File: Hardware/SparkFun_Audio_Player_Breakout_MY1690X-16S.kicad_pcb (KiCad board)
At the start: 4 copper layers, 25.4 x 25.4 mm, 67 parts, among them J1 3.5mm TRRS, J2 Conn_01x03, J3 Conn_01x02, J4 USB_C_Receptacle, J5 Conn_01x06, J6 microSD, Q1 BSS138, U2 MY1690X-16S

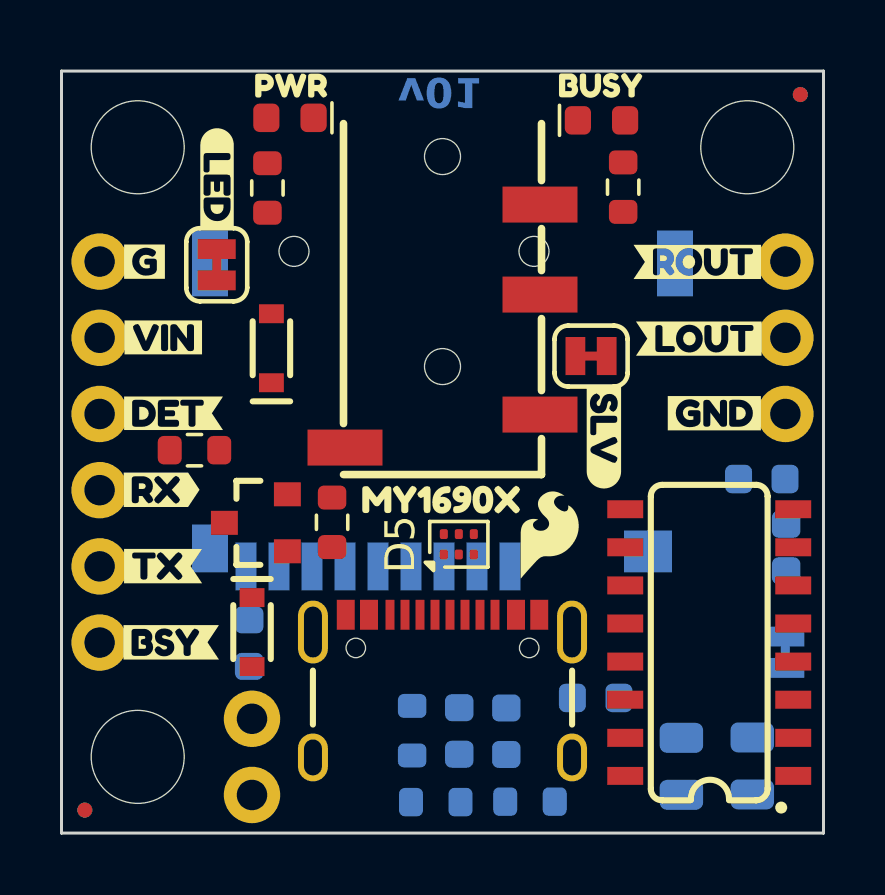
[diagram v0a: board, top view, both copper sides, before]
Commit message: re-order header pins to put GND/VIN/RX/TX in a row
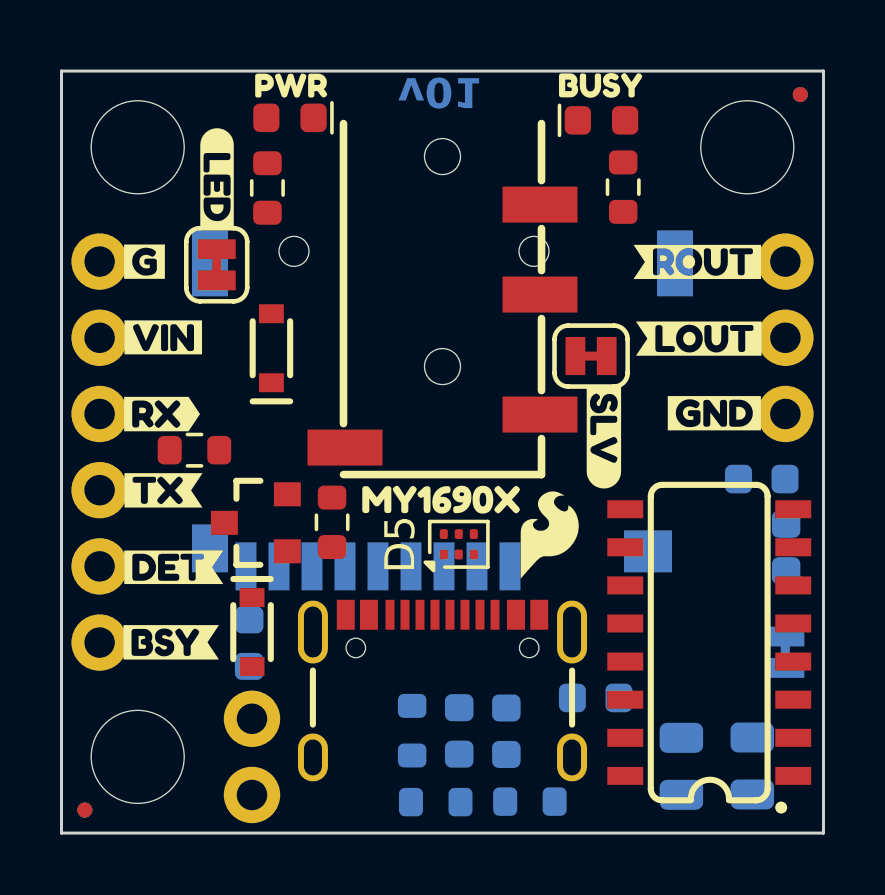
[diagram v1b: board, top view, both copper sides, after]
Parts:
- removed kibuzzard-6792CCC6: G***, kibuzzard-6792CCC6
- added kibuzzard-6793B9F5: G***, kibuzzard-6793B9F5, B.Cu at (137.7, 107.9)
- moved kibuzzard-6792C89C 5.13 mm to (138.4, 108.0)
- moved kibuzzard-6792CCE2 2.56 mm to (138.0, 102.9)
- moved kibuzzard-6792CCF2 2.56 mm to (137.8, 105.4)
- moved kibuzzard-6792C82F 2.52 mm to (138.0, 102.9)
- moved kibuzzard-6792C85C 2.52 mm to (138.0, 105.4)
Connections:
- J5 pad 3: SD_DET -> MY_RX
- J5 pad 4: MY_RX -> MY_TX
- J5 pad 5: MY_TX -> SD_DET

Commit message: TVS diode SOT23-6 package
-for easier production/rework
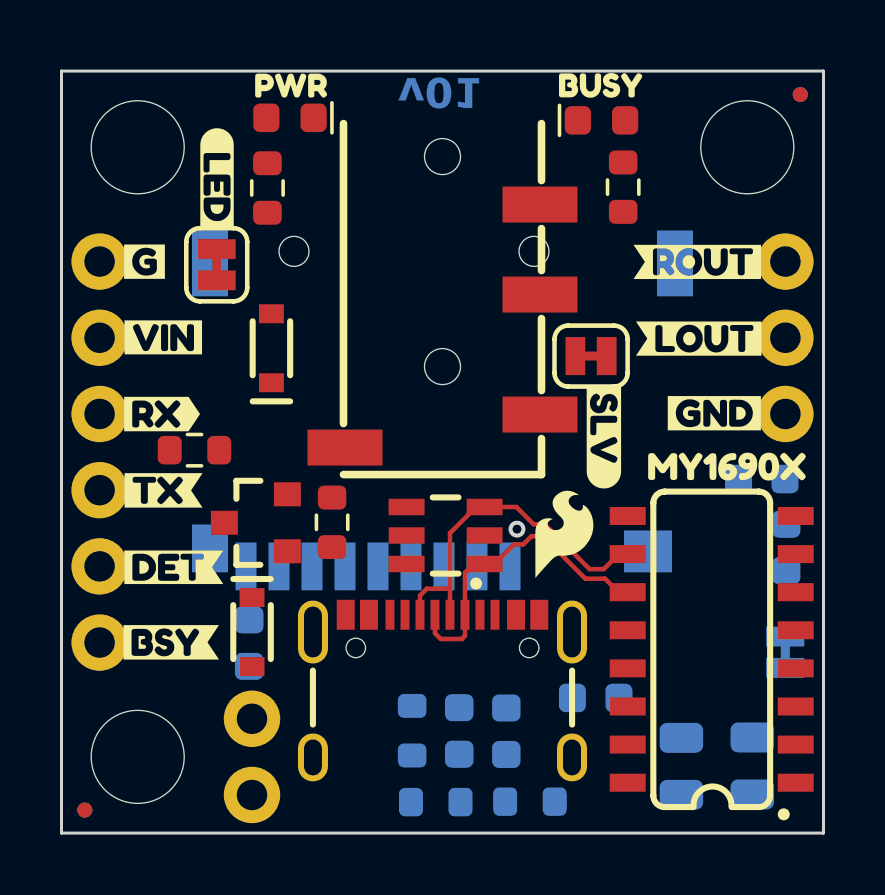
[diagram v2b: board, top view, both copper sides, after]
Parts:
- removed D5: PRTR5V0U2F, Package_TO_SOT_SMD:SOT-886
- added D6: DT1042-04SO, SparkFun-Semiconductor-Standard:SOT23-6, F.Cu at (147.4, 106.9)
- moved kibuzzard-6792C7DD 9.59 mm to (156.8, 104.6)
- moved G*** 0.49 mm to (151.4, 106.9)
- moved U2 0.24 mm to (156.3, 110.7)
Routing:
- net Net-(D6-I/O2): track 0.00 -> 11.8 mm
- net Net-(D6-I/O1): track 0.00 -> 10.5 mm
- net GND: vias 0 -> 1

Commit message: Routed v01 (pre-review)
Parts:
- added C6: 10uF, SparkFun-Capacitor:C_0603_1608Metric, B.Cu at (159.1, 113.6)
- added C9: 0.1uF, SparkFun-Capacitor:C_0603_1608Metric, B.Cu at (157.1, 107.5)
- added kibuzzard-679417DC: G***, kibuzzard-679417DC, F.Cu at (143.3, 98.3)
- moved R4 1.95 mm to (140.8, 103.1), turned to 0 degrees
- moved C4 1.29 mm to (156.4, 114.6)
- moved C5 1.00 mm to (154.3, 114.6)
- moved Q1 0.76 mm to (140.9, 105.8), turned to 90 degrees
- moved R1 0.48 mm to (143.2, 106.7), turned to 90 degrees
- moved C8 0.40 mm to (159.2, 107.4)
- moved C7 0.39 mm to (158.3, 105.2)
- moved C1 0.34 mm to (152.2, 112.0)
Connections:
- JP2 pad 2: 3.3V_P -> VCC
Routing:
- net BUSY: track 0.00 -> 31.9 mm, vias 0 -> 2
- net 3.3V_P: track 0.00 -> 31.8 mm, vias 0 -> 3
- net DAC_R: track 0.00 -> 26.3 mm
- net SD_CLK: track 0.00 -> 25.6 mm, vias 0 -> 1
- net DAC_L: track 0.00 -> 23.3 mm, vias 0 -> 1
- net MY_TX: track 0.00 -> 22.7 mm
- net SD_DAT: track 0.00 -> 20.7 mm, vias 0 -> 1
- net Net-(JP1-A): track 0.00 -> 19.7 mm, vias 0 -> 3
- net MY_RX_LV: track 0.00 -> 18.4 mm
- net Net-(D2-K): track 0.00 -> 16.6 mm, vias 0 -> 2
- net SD_CMD: track 0.00 -> 15.7 mm, vias 0 -> 1
- net Net-(J4-CC2): track 0.00 -> 12.6 mm, vias 0 -> 1
- net VCC: track 0.00 -> 11.7 mm, vias 0 -> 5
- net VUSB: track 0.00 -> 11.2 mm, vias 0 -> 2
- net Net-(JP3-A): track 0.00 -> 8.94 mm
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- added copper zone on F.Cu, net VUSB

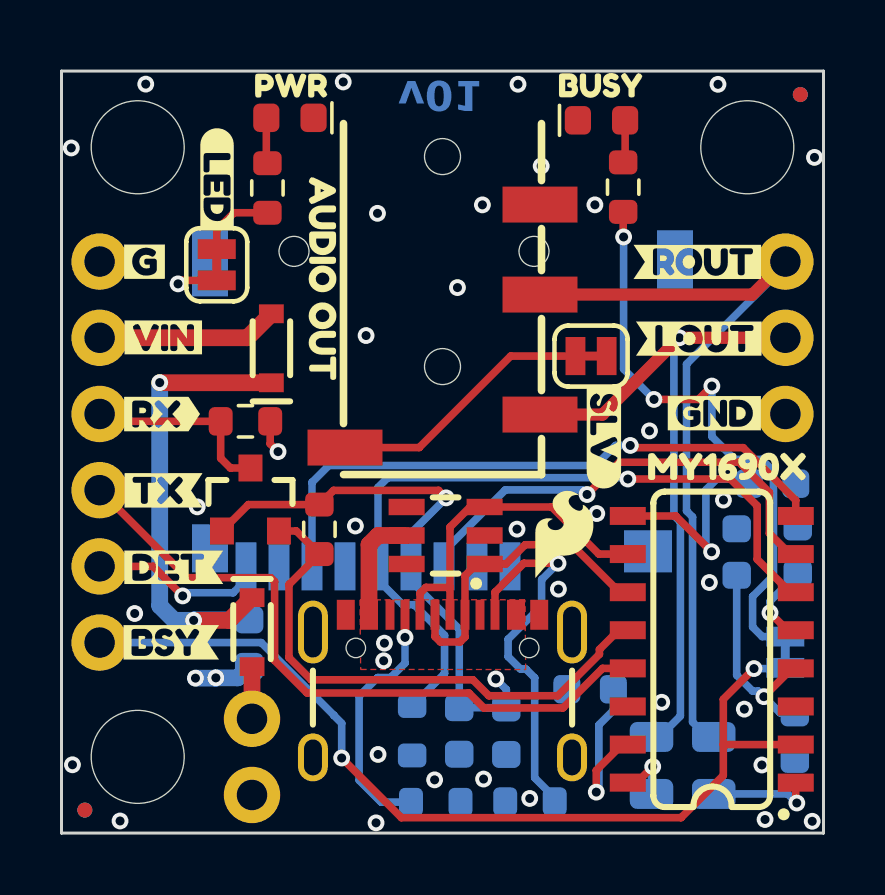
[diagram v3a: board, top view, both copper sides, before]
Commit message: review changes 1
-TX bottom silk fishtail (output)
-centered position of OSHW logo
-nudged vcc vias near VUSB pth headers for better ground flow pour
-named JP3 "SLV"
-added jumper comments to sch
-moved C1/C8 to avoid text overlap in SCH
-added RD to jumpers in sch
-added NC flags to unused pins on SCH
-measures
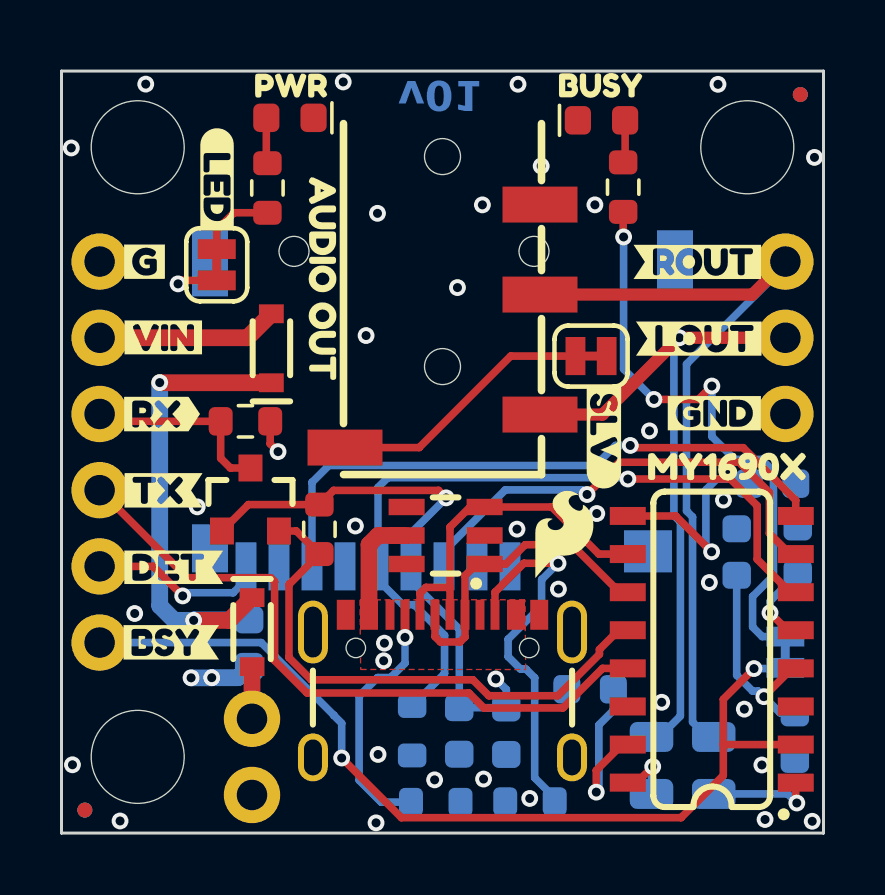
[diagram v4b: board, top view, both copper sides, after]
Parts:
- removed kibuzzard-6792CCF2: G***, kibuzzard-6792CCF2
- added kibuzzard-6798FF71: G***, kibuzzard-6798FF71, B.Cu at (138.0, 105.4)
- JP3: value ~ -> SLV
- moved Ref** 0.15 mm to (147.3, 110.6)
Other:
- board text added: "Inner Copper Weight: 0.5oz"
- board text added: "Layers: 4"
- board text removed: "Layers: 2"

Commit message: removed R6 pull-down on uSD CLK line
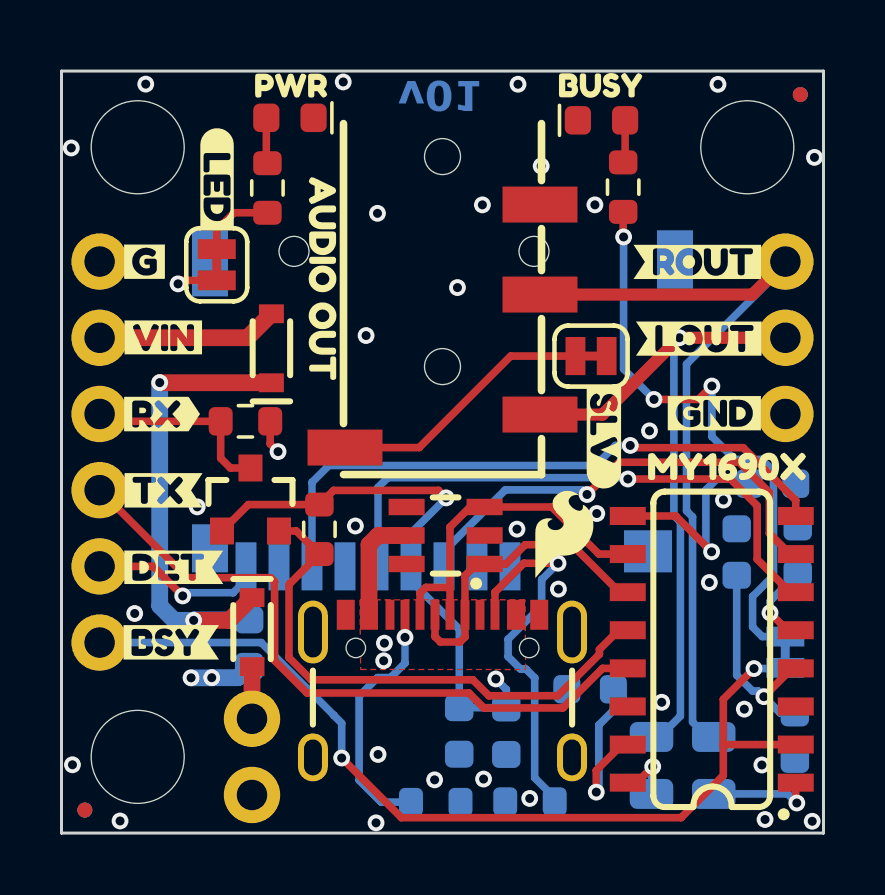
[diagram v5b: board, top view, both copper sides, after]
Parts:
- removed R6: 1k, SparkFun-Resistor:R_0603_1608Metric
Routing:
- net SD_CLK: track 25.6 -> 19.3 mm

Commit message: review changes 2
-rotated LED jumper for easier access to cut when headers are populated
-repositioned bottom passive components under the USB (now that R6 is gone). This allows bypass caps to be closer to uSD card pins.
-updated frame info on brd and sch
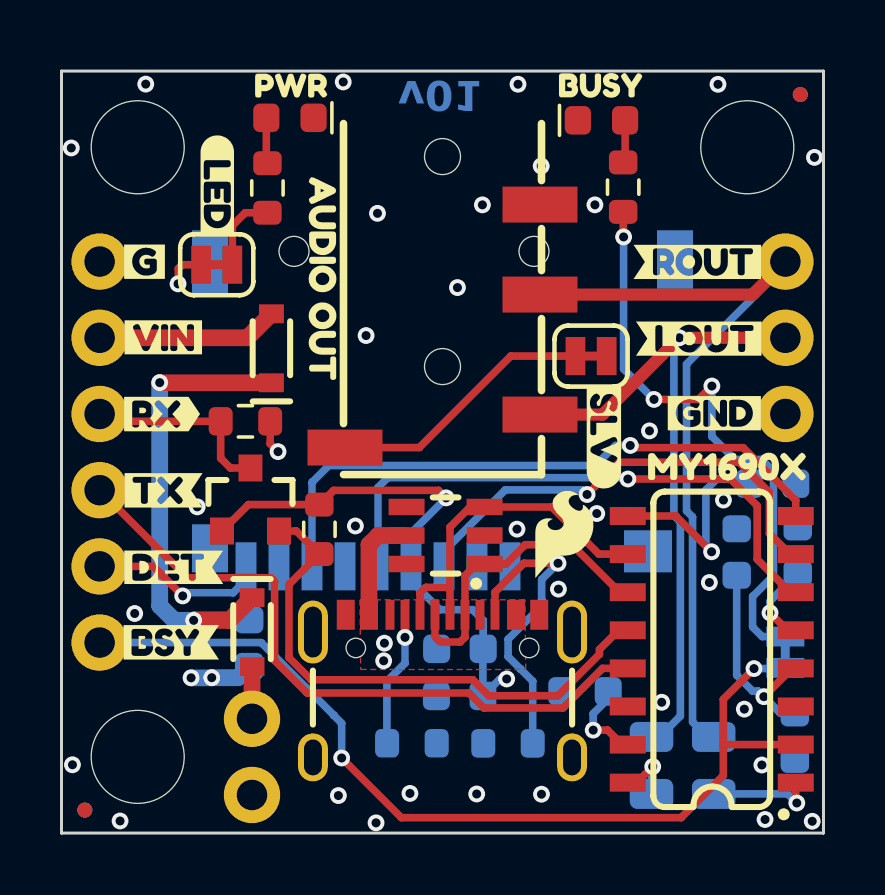
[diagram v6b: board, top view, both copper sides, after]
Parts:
- moved Ref** 5.22 mm to (147.3, 115.8)
- moved C3 2.74 mm to (147.9, 110.7), turned to 180 degrees
- moved R3 2.12 mm to (146.3, 113.8)
- moved R2 2.07 mm to (149.5, 113.8)
- moved C2 1.95 mm to (147.9, 112.3), turned to 180 degrees
- moved G1 1.47 mm to (216.1, 168.0)
- moved kibuzzard-6792CF7B 0.24 mm to (139.8, 95.3)
- moved C1 0.18 mm to (152.1, 112.1)
- turned JP2 to 180 degrees
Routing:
- net Net-(J4-CC1): track 8.43 -> 4.48 mm
- net Net-(U2-VPN): track 5.79 -> 2.99 mm
- net Net-(J4-CC2): track 12.6 -> 10.3 mm
- net 3.3V_P: track 31.8 -> 30.4 mm
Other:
- board text added: "Ordering Notes:"
- board text added: "Solder Mask: Black"
- board text removed: "Ordering Notes"
- board text removed: "Solder Mask: Red"

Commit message: repositioned connectors to have over-hang
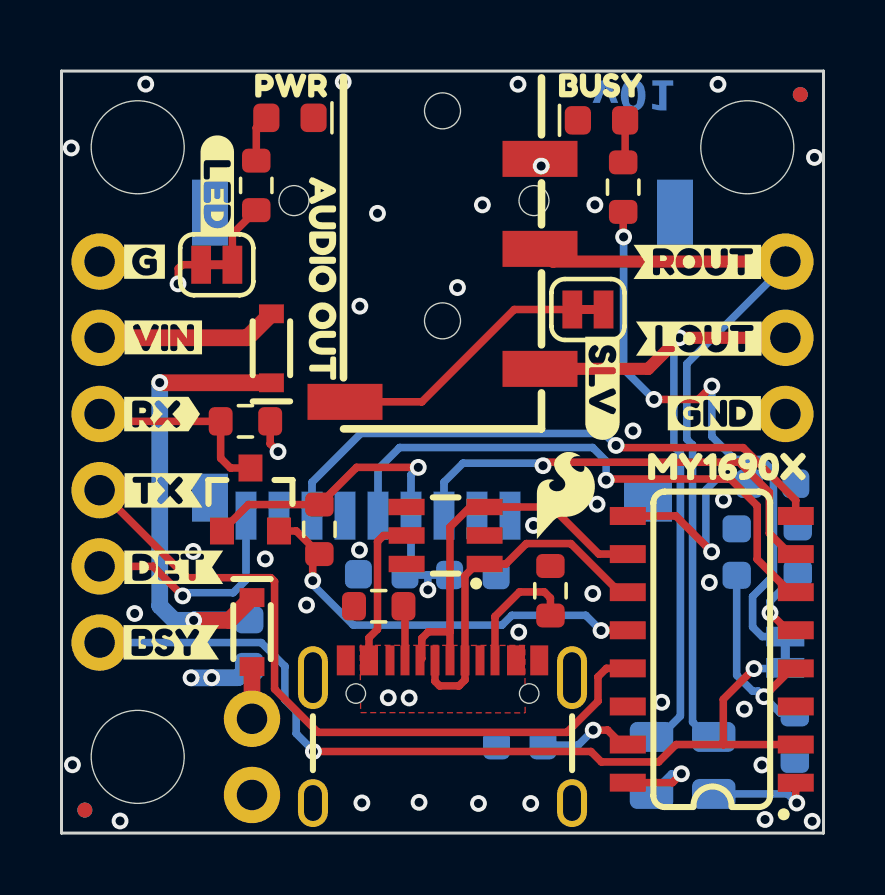
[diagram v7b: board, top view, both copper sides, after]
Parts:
- R2, R3: moved to F.Cu
- moved R2 5.28 mm to (150.9, 108.8), turned to 90 degrees
- moved R3 4.70 mm to (145.2, 109.3), turned to 0 degrees
- moved Ref** 4.68 mm to (147.3, 111.1)
- moved C2 4.05 mm to (148.3, 108.2), turned to 0 degrees
- moved C3 3.60 mm to (145.3, 108.2)
- moved C1 2.82 mm to (149.9, 113.9)
- moved kibuzzard-6792CAD9 2.07 mm to (145.2, 114.8)
- moved kibuzzard-6792CAB7 1.99 mm to (145.5, 113.4)
- moved J6 1.69 mm to (147.3, 95.8)
- moved kibuzzard-6792CF8E 1.62 mm to (152.7, 102.0)
- moved JP3 1.56 mm to (152.2, 99.4), turned to 180 degrees
- moved J1 1.52 mm to (147.3, 96.3)
- moved J4 1.52 mm to (147.3, 110.7)
- moved G*** 1.30 mm to (151.4, 105.6)
- moved R9 0.38 mm to (141.1, 95.3)
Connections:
- J1 pad S: Net-(JP3-A) -> Net-(JP3-B)
- JP3 pad 1: Net-(JP3-A) -> GND
- JP3 pad 2: GND -> Net-(JP3-B)
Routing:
- net Net-(JP3-A): track 8.94 -> 0.00 mm
- net Net-(JP3-B): track 0.00 -> 8.85 mm
- net Net-(J4-CC2): track 10.3 -> 4.32 mm, vias 1 -> 0
- net MY_RX_LV: track 18.4 -> 14.2 mm, vias 0 -> 2
- net VUSB: track 11.2 -> 15.2 mm
- net Net-(J4-CC1): track 4.48 -> 1.83 mm, vias 1 -> 0
- net 3.3V_P: track 30.4 -> 28.5 mm
- net BUSY: track 31.9 -> 30.2 mm
- net MY_TX: track 22.7 -> 24.4 mm
- net SD_DET: track 5.96 -> 7.65 mm
- net Net-(D6-I/O2): track 11.6 -> 13.1 mm
- net Net-(D6-I/O1): track 10.4 -> 11.9 mm
- net SD_DAT: track 20.7 -> 19.4 mm
- net Net-(U2-DACL): track 1.98 -> 3.19 mm
- net DAC_L: track 23.3 -> 22.6 mm
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- added copper zone on In1.Cu, net VUSB

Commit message: checklist eng run
-added ordering instruction about NPTH holes (under the TRRS connector)
-sch cleanup
-add VIN range in SCH and BRD
-add "1234" text objects to each layer
-nudges a via under LOUT silk
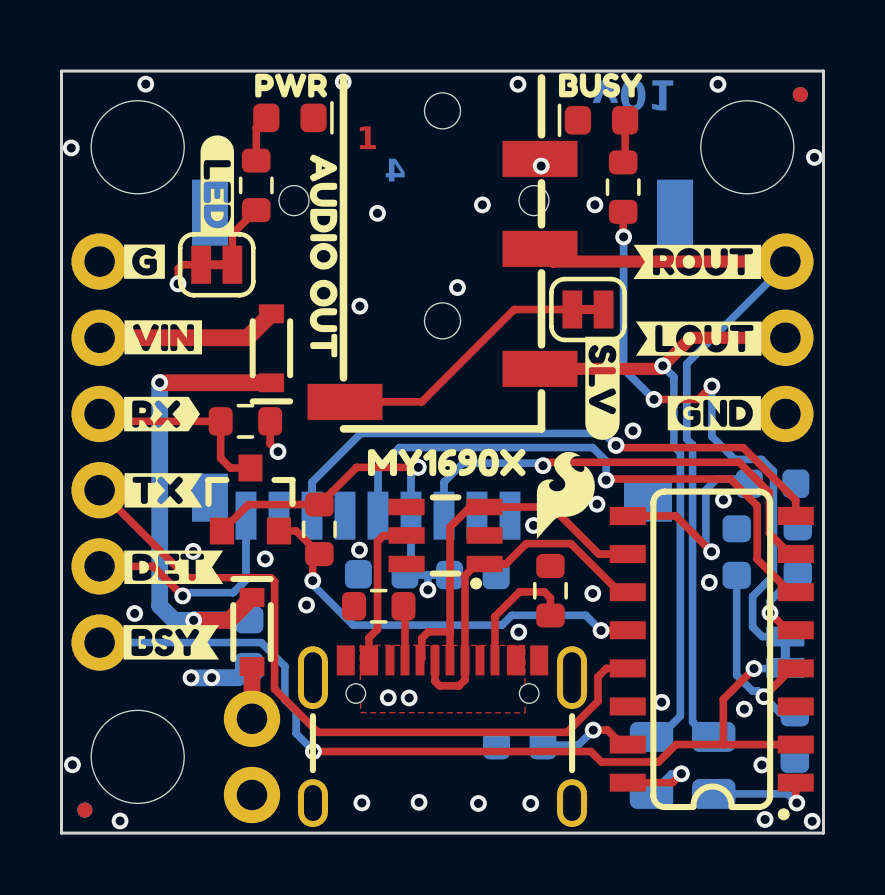
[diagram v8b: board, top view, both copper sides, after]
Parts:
- added kibuzzard-679A5CF8: G***, kibuzzard-679A5CF8, B.Cu at (147.2, 109.6)
- moved kibuzzard-6792C7DD 9.34 mm to (147.5, 104.5)
- moved kibuzzard-679417DC 0.75 mm to (143.4, 97.6)
- moved Ref** 0.64 mm to (147.3, 111.8)
- moved kibuzzard-6792CF5F 0.60 mm to (155.7, 111.4)
- moved kibuzzard-6792CAD9 0.24 mm to (145.2, 115.0)
- moved kibuzzard-6792CAB7 0.21 mm to (145.5, 113.7)
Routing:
- net DAC_L: track 22.6 -> 21.8 mm
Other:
- board text added: "1"
- board text added: "2"
- board text added: "3"
- board text added: "4"
- board text added: "NPTH (NON PLATED THROUGH HOLE) Drills: 1.2mm dia (0.0472 inch dia) ALL OTHER DRILLS PLATED THROUGH HOLE"
